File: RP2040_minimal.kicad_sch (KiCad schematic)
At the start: 37 parts, among them J1 Conn_02x05_Odd_Even, J2 Conn_01x02, J3 Conn_01x02, U1 LM4040DBZ-3, U2 W25Q128JVS, U3 RP2040, U4 LM4040DBZ-3, Y1 ABLS-12.000MHZ-B4-T, Y2 X322516MLB4SI

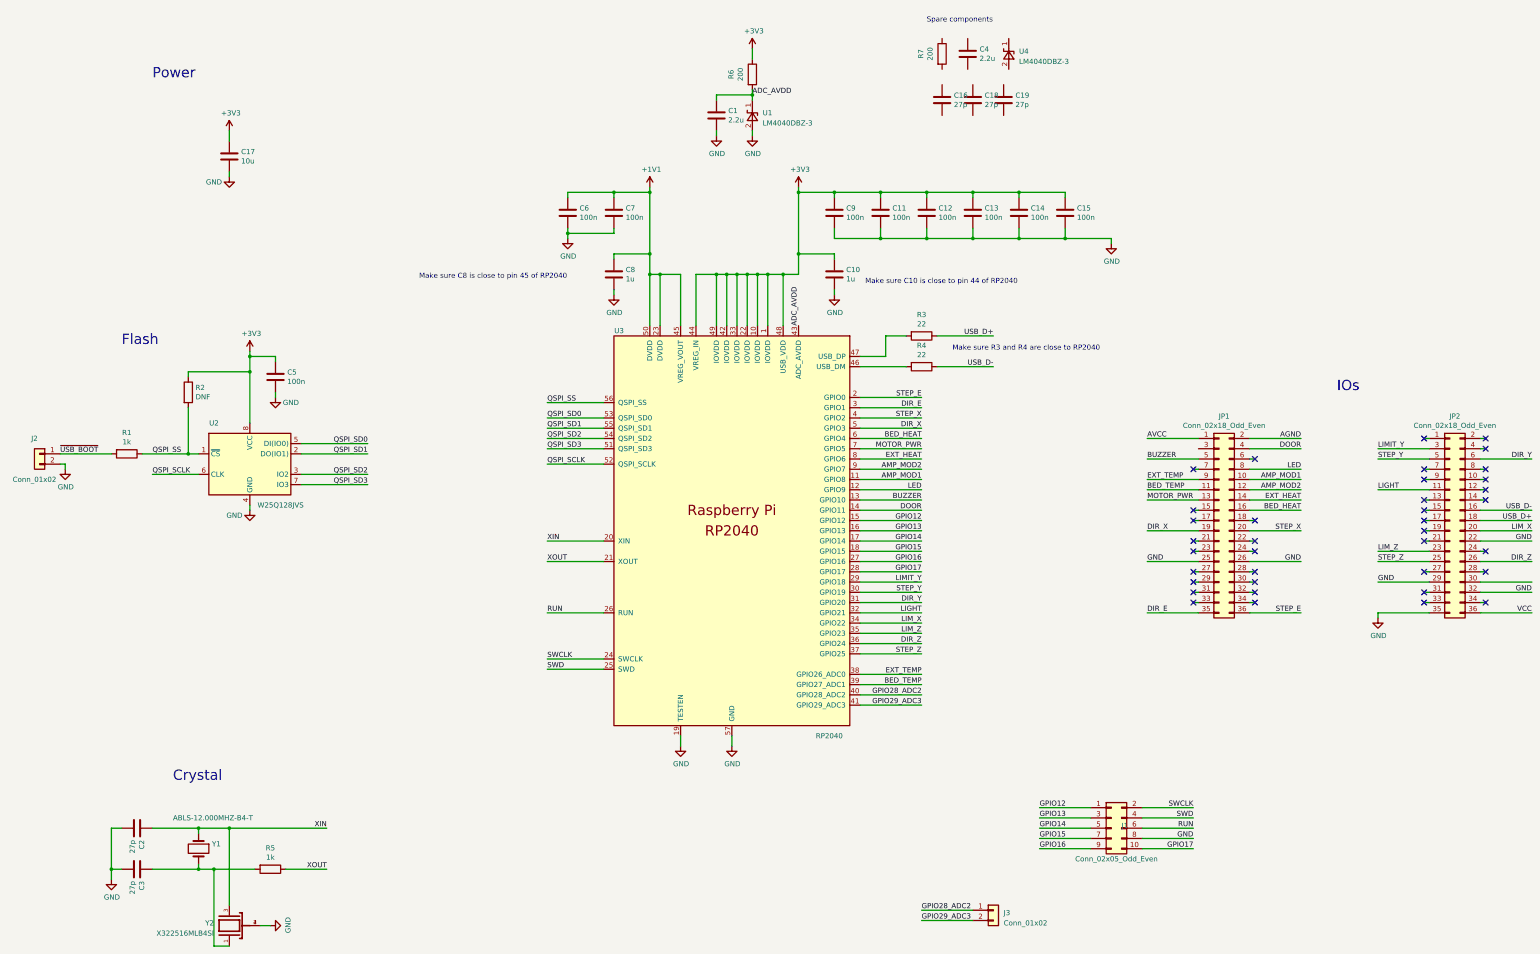
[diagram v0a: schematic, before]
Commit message: Board ready for production, tab on bottom
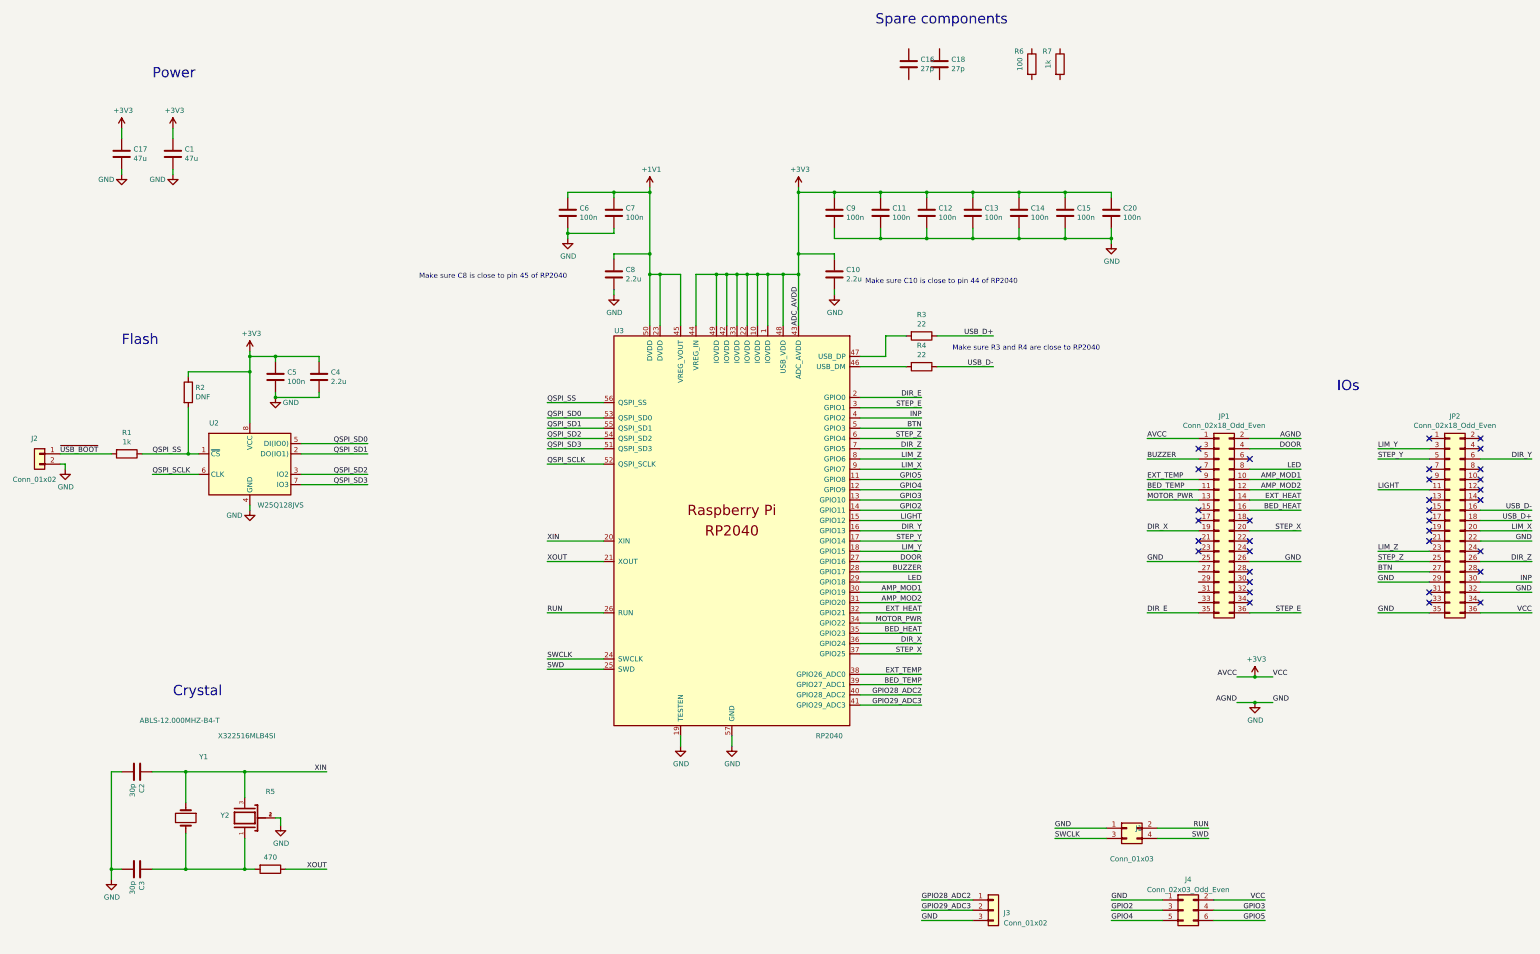
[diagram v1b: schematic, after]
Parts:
- removed C19: 27p, Capacitor_SMD:C_0402_1005Metric, symbol Device:C
- removed U1, U4: LM4040DBZ-3, Package_TO_SOT_SMD:SOT-23, symbol Reference_Voltage:LM4040DBZ-3
- added C20: 100n, Capacitor_SMD:C_0402_1005Metric, symbol Device:C
- added J4: Conn_02x03_Odd_Even, Connector_PinHeader_2.54mm:PinHeader_2x03_P2.54mm_Vertical, symbol Connector_Generic:Conn_02x03_Odd_Even
- C1: value 2.2u -> 47u; footprint Capacitor_SMD:C_0402_1005Metric -> Capacitor_SMD:C_0805_2012Metric
- C10, C8: value 1u -> 2.2u
- C17: value 10u -> 47u
- C2, C3: value 27p -> 30p
- J1: value Conn_02x05_Odd_Even -> Conn_01x03; footprint Connector_PinHeader_2.54mm:PinHeader_2x05_P2.54mm_Vertical -> Connector_PinHeader_2.54mm:PinHeader_2x02_P2.54mm_Vertical; symbol Connector_Generic:Conn_02x05_Odd_Even -> Connector_Generic:Conn_02x02_Odd_Even
- J3: footprint Connector_PinHeader_2.54mm:PinHeader_1x02_P2.54mm_Vertical -> Connector_PinHeader_2.54mm:PinHeader_1x03_P2.54mm_Vertical; symbol Connector_Generic:Conn_01x02 -> Connector_Generic:Conn_01x03
- JP1: footprint Connector_PinHeader_2.54mm:PinHeader_2x18_P2.54mm_Vertical -> RP2040_minimal:PinHeader_2x18_P2.54mm_Vertical_backside
- JP2: footprint Connector_PinHeader_2.54mm:PinHeader_2x18_P2.54mm_Vertical -> RP2040_minimal:PinHeader_2x18_P2.54mm_Vertical_backside_pads15+17_removed
- R5: value 1k -> 470
- R6: value 200 -> 100
- R7: value 200 -> 1k
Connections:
- net AGND is gone; now on net GND: JP1.2 (Pin_2)
- net AVCC is gone; now on net +3V3: JP1.1 (Pin_1)
- net VCC is gone; now on net +3V3: JP2.36 (Pin_36)
- net +3V3: now also C1.1, C4.1, U3.43 (ADC_AVDD), C20.1, J4.2 (Pin_2); no longer R6.1
- net AMP_MOD1: now also U3.30 (GPIO19); no longer U3.11 (GPIO8)
- net AMP_MOD2: now also U3.31 (GPIO20); no longer U3.9 (GPIO7)
- net BED_HEAT: now also U3.35 (GPIO23); no longer U3.6 (GPIO4)
- net BUZZER: now also U3.28 (GPIO17); no longer U3.13 (GPIO10)
- net DIR_E: now also U3.2 (GPIO0); no longer U3.3 (GPIO1)
- net DIR_X: now also U3.36 (GPIO24); no longer U3.5 (GPIO3)
- net DIR_Y: now also U3.16 (GPIO13); no longer U3.31 (GPIO20)
- net DIR_Z: now also U3.7 (GPIO5); no longer U3.36 (GPIO24)
- net DOOR: now also U3.27 (GPIO16); no longer U3.14 (GPIO11)
- net EXT_HEAT: now also U3.32 (GPIO21); no longer U3.8 (GPIO6)
- net GND: now also C4.2, J1.1 (Pin_1), J3.3 (Pin_3), C20.2, J4.1 (Pin_1); no longer J1.8 (Pin_8)
- net LED: now also U3.29 (GPIO18); no longer U3.12 (GPIO9)
- net LIGHT: now also U3.15 (GPIO12); no longer U3.32 (GPIO21)
- net LIM_X: now also U3.9 (GPIO7); no longer U3.34 (GPIO22)
- net LIM_Z: now also U3.8 (GPIO6); no longer U3.35 (GPIO23)
- net MOTOR_PWR: now also U3.34 (GPIO22); no longer U3.7 (GPIO5)
- net RUN: now also J1.2 (Pin_2); no longer J1.6 (Pin_6)
- net STEP_E: now also U3.3 (GPIO1); no longer U3.2 (GPIO0)
- net STEP_X: now also U3.37 (GPIO25); no longer U3.4 (GPIO2)
- net STEP_Y: now also U3.17 (GPIO14); no longer U3.30 (GPIO19)
- net STEP_Z: now also U3.6 (GPIO4); no longer U3.37 (GPIO25)
- net SWCLK: now also J1.3 (Pin_3); no longer J1.2 (Pin_2)
- net BTN: now reaches JP2.27 (Pin_27)
- net BTN: now also U3.5 (GPIO3)
- net INP: now reaches JP2.30 (Pin_30)
- net INP: now also U3.4 (GPIO2)
- removed net ADC_AVDD: C1.1, R6.2, U3.43 (ADC_AVDD)
- removed net GPIO12: J1.1 (Pin_1), U3.15 (GPIO12)
- removed net GPIO13: J1.3 (Pin_3), U3.16 (GPIO13)
- removed net GPIO14: J1.5 (Pin_5), U3.17 (GPIO14)
- net GPIO15 renamed LIM_Y
- net LIM_Y: now also JP2.3 (Pin_3); no longer J1.7 (Pin_7)
- removed net GPIO16: J1.9 (Pin_9), U3.27 (GPIO16)
- removed net GPIO17: J1.10 (Pin_10), U3.28 (GPIO17)
- removed net LIMIT_Y: JP2.3 (Pin_3), U3.29 (GPIO18)
- new net GPIO2: J4.3 (Pin_3), U3.14 (GPIO11)
- new net GPIO3: J4.4 (Pin_4), U3.13 (GPIO10)
- new net GPIO4: J4.5 (Pin_5), U3.12 (GPIO9)
- new net GPIO5: J4.6 (Pin_6), U3.11 (GPIO8)
- no-connect marks 37 -> 33
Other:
- moved on the sheet: C16, C17, C18, C2, Y1, Y2
